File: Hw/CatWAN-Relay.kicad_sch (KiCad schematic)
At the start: 47 parts, among them J10 USB_B, J2 INPUTS, J3 OUTPUTS, J4 SWD, J5 Serial, Q1 MMBT2222A, Q2 MMBT2222A, Q3 MMBT2222A, SW1 RST, U1 ATSAMD21E, U2 RFM95W-915-868, U3 LTV-817, U4 LTV-817, U5 LTV-817, U6 LM2596_DC-DC, U7 AP2114H-3.3TRG1, Y1 UD2-3NU, Y2 UD2-3NU, Y3 UD2-3NU

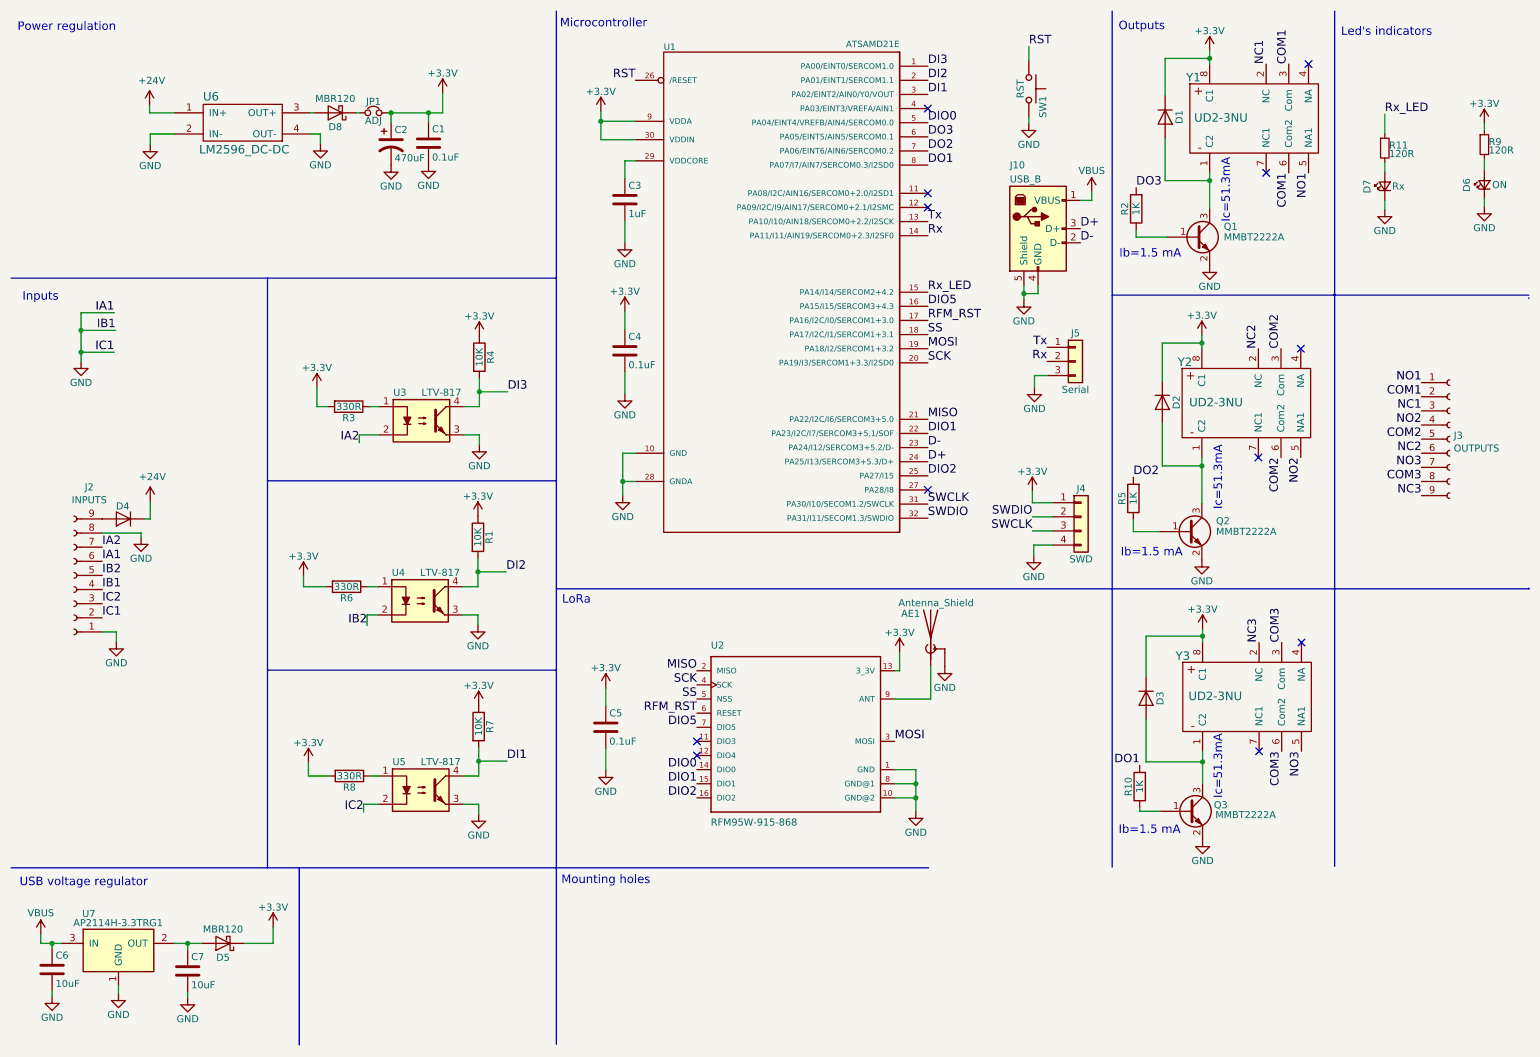
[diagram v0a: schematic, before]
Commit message: feat: init CatWan relay 2
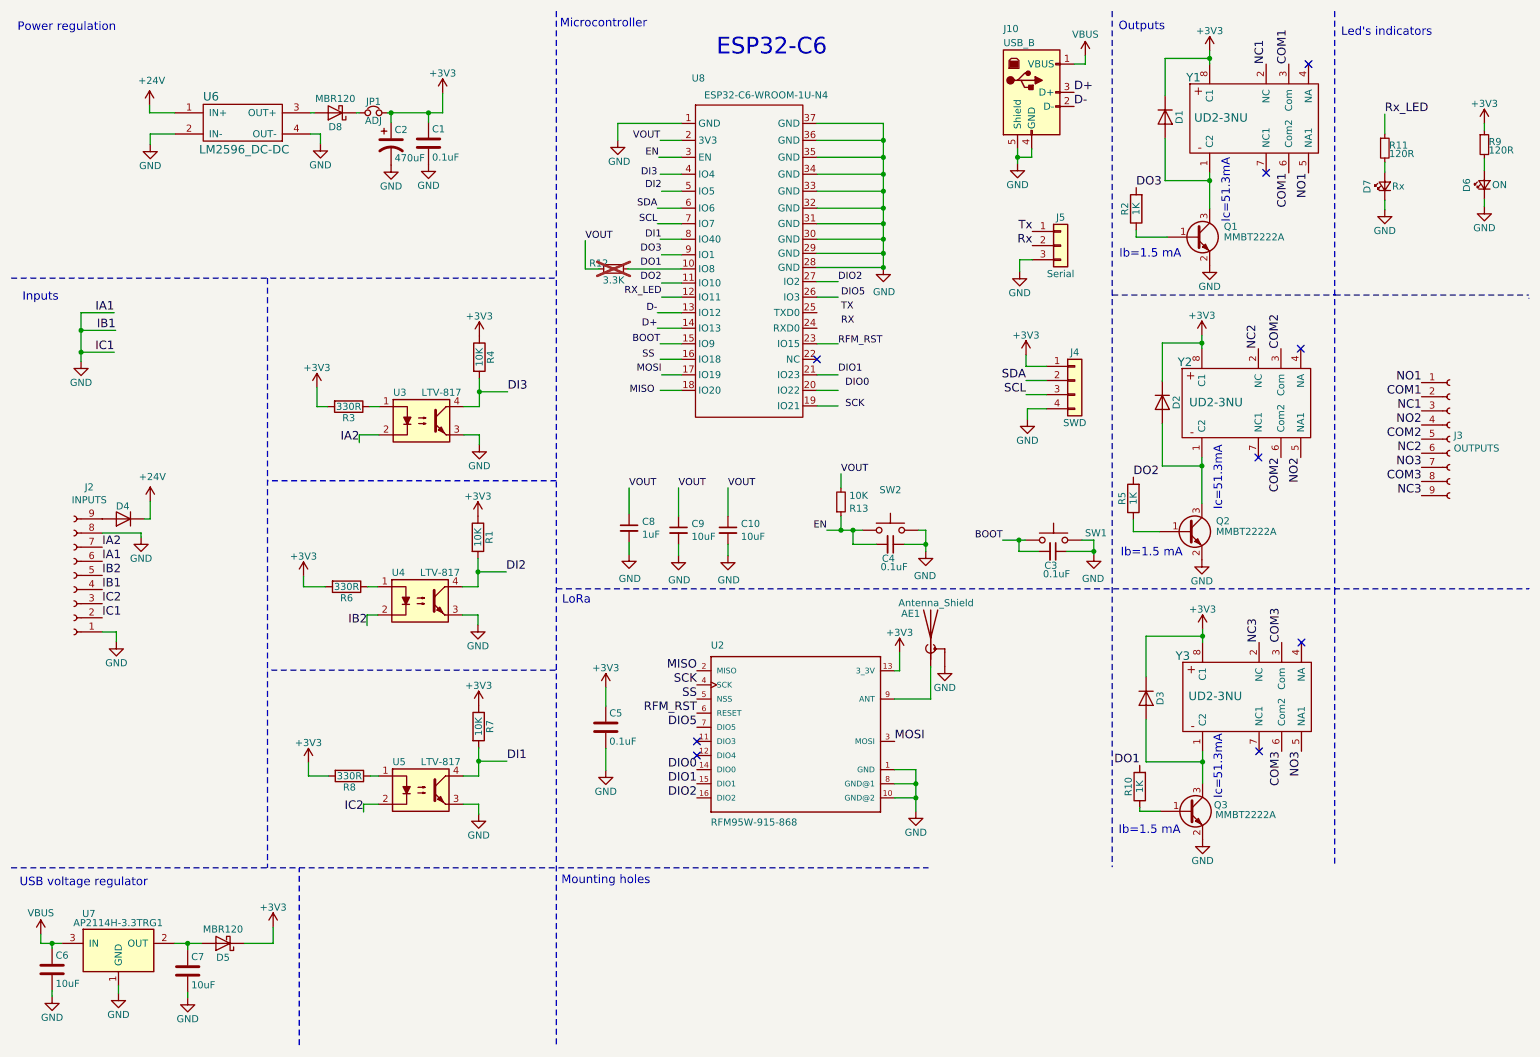
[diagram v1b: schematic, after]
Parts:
- removed C3: 1uF, Capacitor_SMD:C_0805_2012Metric_Pad1.15x1.40mm_HandSolder, symbol CatWAN-Relay-rescue:C-agroin-rescue
- removed C4: 0.1uF, Capacitor_SMD:C_0805_2012Metric_Pad1.15x1.40mm_HandSolder, symbol CatWAN-Relay-rescue:C-agroin-rescue
- removed SW1: RST, Button_Switch_SMD:SW_SPST_TL3342, symbol CatWAN-Relay-rescue:SW_Push-agroin-rescue
- removed U1: ATSAMD21E, Package_QFP:TQFP-32_7x7mm_P0.8mm, symbol CatWAN-Relay-rescue:ATSAMD21E-agroin-rescue
- added C10, C9: 10uF, Capacitor_SMD:C_0603_1608Metric, symbol Device:C_Small
- added C3, C4: 0.1uF, Capacitor_SMD:C_0603_1608Metric, symbol Device:C_Small
- added C8: 1uF, Capacitor_SMD:C_0603_1608Metric, symbol Device:C_Small
- added R12: 3.3K, Resistor_SMD:R_0603_1608Metric, symbol Device:R_Small
- added R13: 10K, Resistor_SMD:R_0603_1608Metric, symbol Device:R_Small
- added SW1, SW2: ~, Button_Switch_SMD:SW_SPST_TL3342, symbol Switch:SW_Push
- added U8: ESP32-C6-WROOM-1U-N4, Library:XCVR_ESP32-C6-WROOM-1-N8, symbol Minino:ESP32-C6-WROOM-1U-N8
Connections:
- net D+: now also U8.14 (IO13)
- net D-: now also U8.13 (IO12)
- net DI1: now also U8.8 (IO40)
- net DIO2: now also U8.27 (IO2)
- net GND: now also C10.2, C3.1, C4.1, C8.2, C9.2, SW1.1, SW2.1, U8.1 (GND), U8.28 (GND), U8.29 (GND), U8.30 (GND), U8.31 (GND), U8.32 (GND), U8.33 (GND), U8.34 (GND), U8.35 (GND), U8.36 (GND), U8.37 (GND)
- net SWCLK renamed SCL
- net SCL: now also U8.7 (IO7)
- net SWDIO renamed SDA
- net SDA: now also U8.6 (IO6)
- new net: R12.1, U8.10 (IO8)
- new net BOOT: C3.2, SW1.2, U8.15 (IO9)
- new net EN: C4.2, R13.1, SW2.2, U8.3 (EN)
- new net VOUT: C10.1, C8.1, C9.1, R12.2, R13.2, U8.2 (3V3)
- no-connect marks 12 -> 9
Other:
- note added: "ESP32-C6"
- moved on the sheet: J10, J4, J5

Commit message: feat(Hw):Update_sch_aadded_footprints_symbols
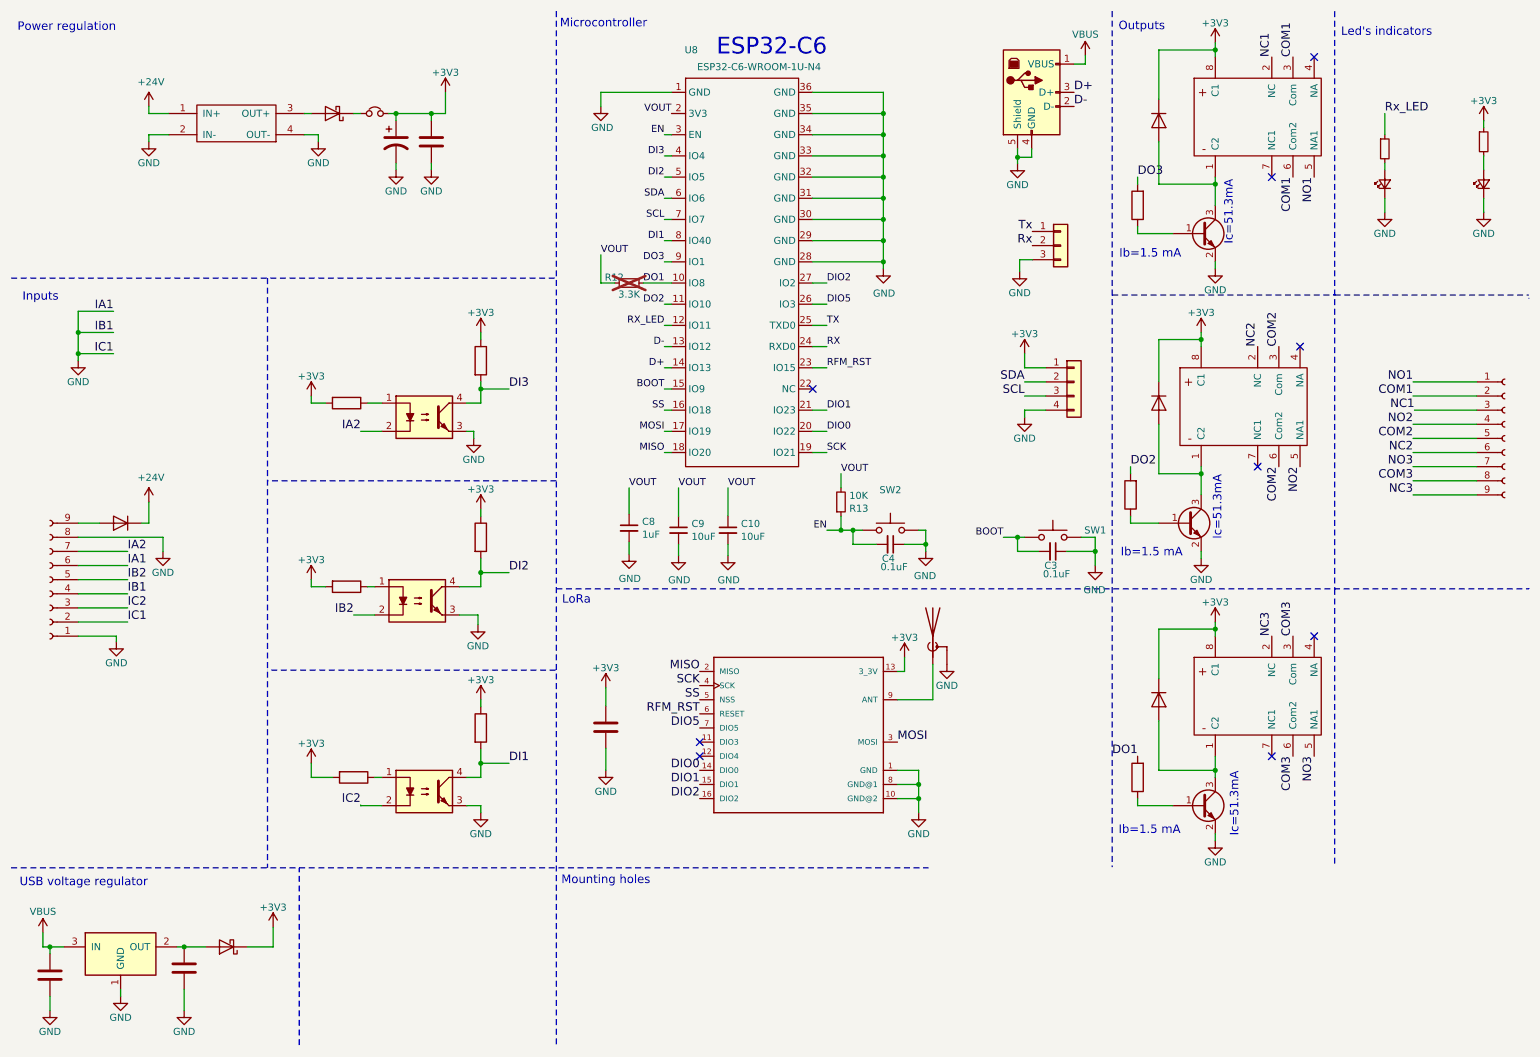
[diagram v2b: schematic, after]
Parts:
- AE1: footprint Connectors:MOLEX_1661 -> Connector_Coaxial:U.FL_Molex_MCRF_73412-0110_Vertical
- C1, C5, C6, C7: footprint Capacitor_SMD:C_0805_2012Metric_Pad1.15x1.40mm_HandSolder -> Capacitor_SMD:C_0603_1608Metric
- J10: footprint USB:629105150521 -> agroin:C393939
- R1, R10, R11, R2, R3, R4, R5, R6, R7, R8, R9: footprint Resistor_SMD:R_0805_2012Metric_Pad1.15x1.40mm_HandSolder -> Resistor_SMD:R_0603_1608Metric
- U8: footprint Library:XCVR_ESP32-C6-WROOM-1-N8 -> agroin:XCVR_ESP32-C6-WROOM-1-N8
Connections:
- net DI2: now also U8.5 (IO5)
- net DI3: now also U8.4 (IO4)
- net DIO0: now also U8.20 (IO22)
- net DIO1: now also U8.21 (IO23)
- net DIO5: now also U8.26 (IO3)
- net DO1: now also R12.1, U8.10 (IO8)
- net DO2: now also U8.11 (IO10)
- net DO3: now also U8.9 (IO1)
- net MISO: now also U8.18 (IO20)
- net MOSI: now also U8.17 (IO19)
- net RFM_RST: now also U8.23 (IO15)
- net RX: now also U8.24 (RXD0)
- net RX_LED: now also U8.12 (IO11)
- net SCK: now also U8.19 (IO21)
- net SS: now also U8.16 (IO18)
- net TX: now also U8.25 (TXD0)
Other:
- moved on the sheet: R12, SW1

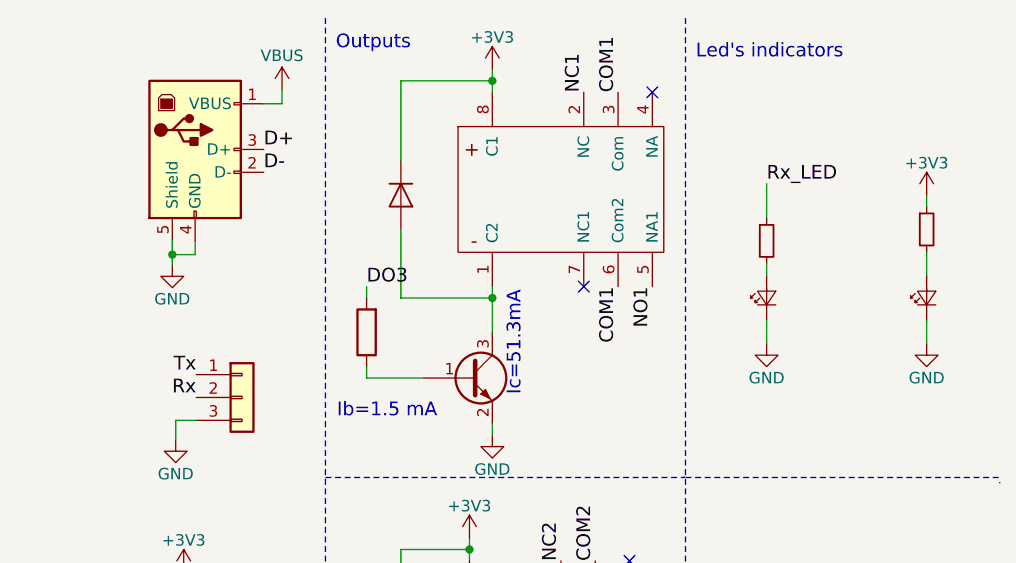
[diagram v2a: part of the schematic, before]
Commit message: fix: labels tx, rx and rx_leds
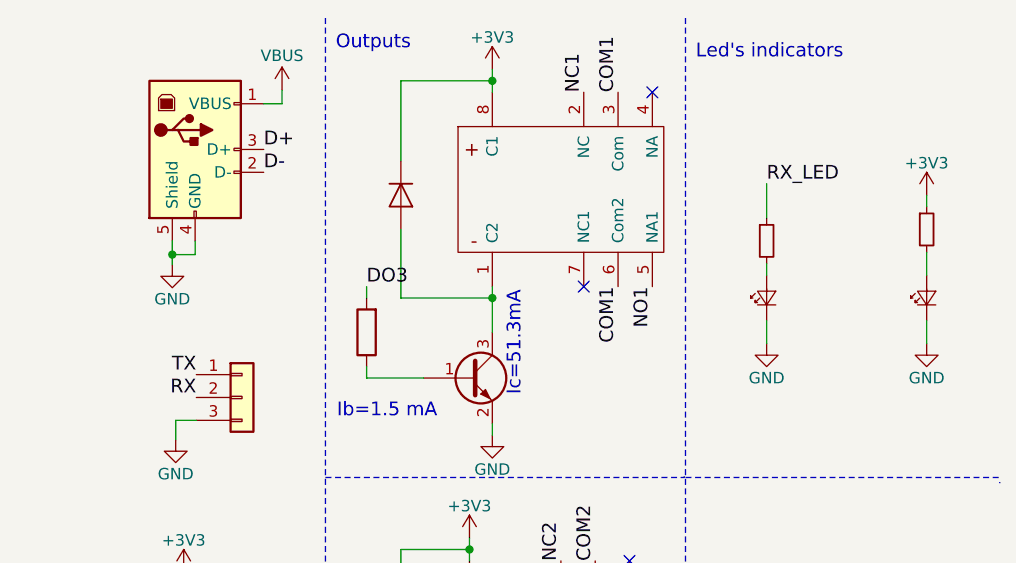
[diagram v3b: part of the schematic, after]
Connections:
- net Rx is gone; now on net RX: J5.2 (Pin_2)
- net Rx_LED is gone; now on net RX_LED: R11.1
- net Tx is gone; now on net TX: J5.1 (Pin_1)
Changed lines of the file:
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@@
 		)
 	)
-	(label "Rx"
+	(label "RX"
 		(at 195.707 54.229 180)
 		(fields_autoplaced yes)
@@
 		)
 	)
-	(label "Rx_LED"
+	(label "RX_LED"
 		(at 259.08 30.48 0)
 		(fields_autoplaced yes)
@@
 		)
 	)
-	(label "Tx"
+	(label "TX"
 		(at 195.707 51.689 180)
 		(fields_autoplaced yes)
